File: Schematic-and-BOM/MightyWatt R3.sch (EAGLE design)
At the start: 93 parts, among them IC1 TLV271IDBVR, IC2 MAX4619EUE, IC3 OPA365AIDBVR, IC4 TS5A3166, IC5 INA225, IC6 ADS1115IDGST, IC7 TLV2372IDGK, IC8 AD5691RAD5691R, IC9 LM2766M6, T1 IXTH75N10L2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

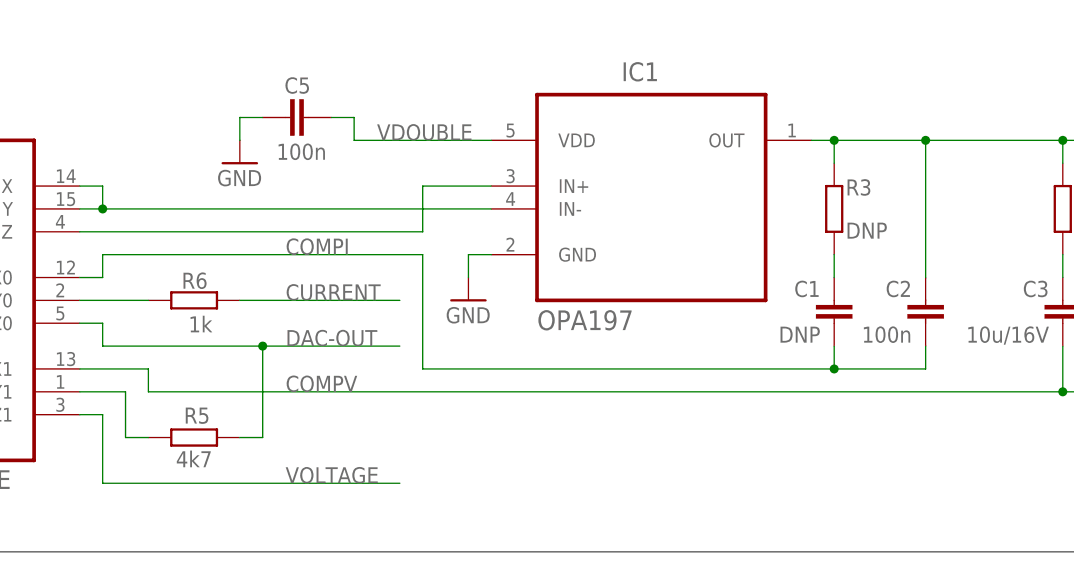
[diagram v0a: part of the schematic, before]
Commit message: Fixed schematic
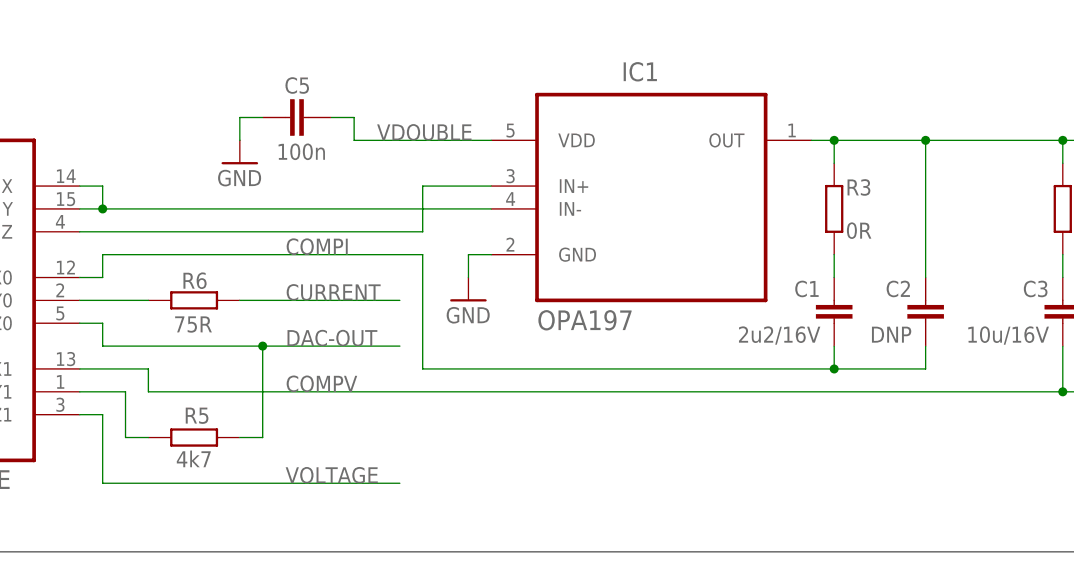
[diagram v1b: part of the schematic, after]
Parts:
- C1: value DNP -> 2u2/16V
- C2: value 100n -> DNP
- R3: value DNP -> 0R
- R6: value 1k -> 75R
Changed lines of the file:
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@@
 <part name="X1" library="con-wago-500-modified" deviceset="W237-4" device=""/>
 <part name="R5" library="rcl" deviceset="R-EU_" device="R0603" value="4k7"/>
-<part name="R6" library="rcl" deviceset="R-EU_" device="R0603" value="1k"/>
+<part name="R6" library="rcl" deviceset="R-EU_" device="R0603" value="75R"/>
 <part name="IC8" library="r2.5-3" deviceset="AD5691R" device="AD5691R"/>
 <part name="VREF1" library="supply2" deviceset="+UB" device=""/>
@@
 <part name="IC2" library="kaktus" deviceset="MAX4619EUE" device=""/>
 <part name="GND30" library="supply1" deviceset="GND" device=""/>
-<part name="C2" library="rcl" deviceset="C-EU" device="C0603" value="100n"/>
-<part name="R3" library="rcl" deviceset="R-EU_" device="R0603" value="DNP"/>
-<part name="C1" library="rcl" deviceset="C-EU" device="C1206" value="DNP"/>
+<part name="C2" library="rcl" deviceset="C-EU" device="C0603" value="DNP"/>
+<part name="R3" library="rcl" deviceset="R-EU_" device="R0603" value="0R"/>
+<part name="C1" library="rcl" deviceset="C-EU" device="C1206" value="2u2/16V"/>
 <part name="VCC1" library="supply1" deviceset="VCCIO" device=""/>
 </parts>

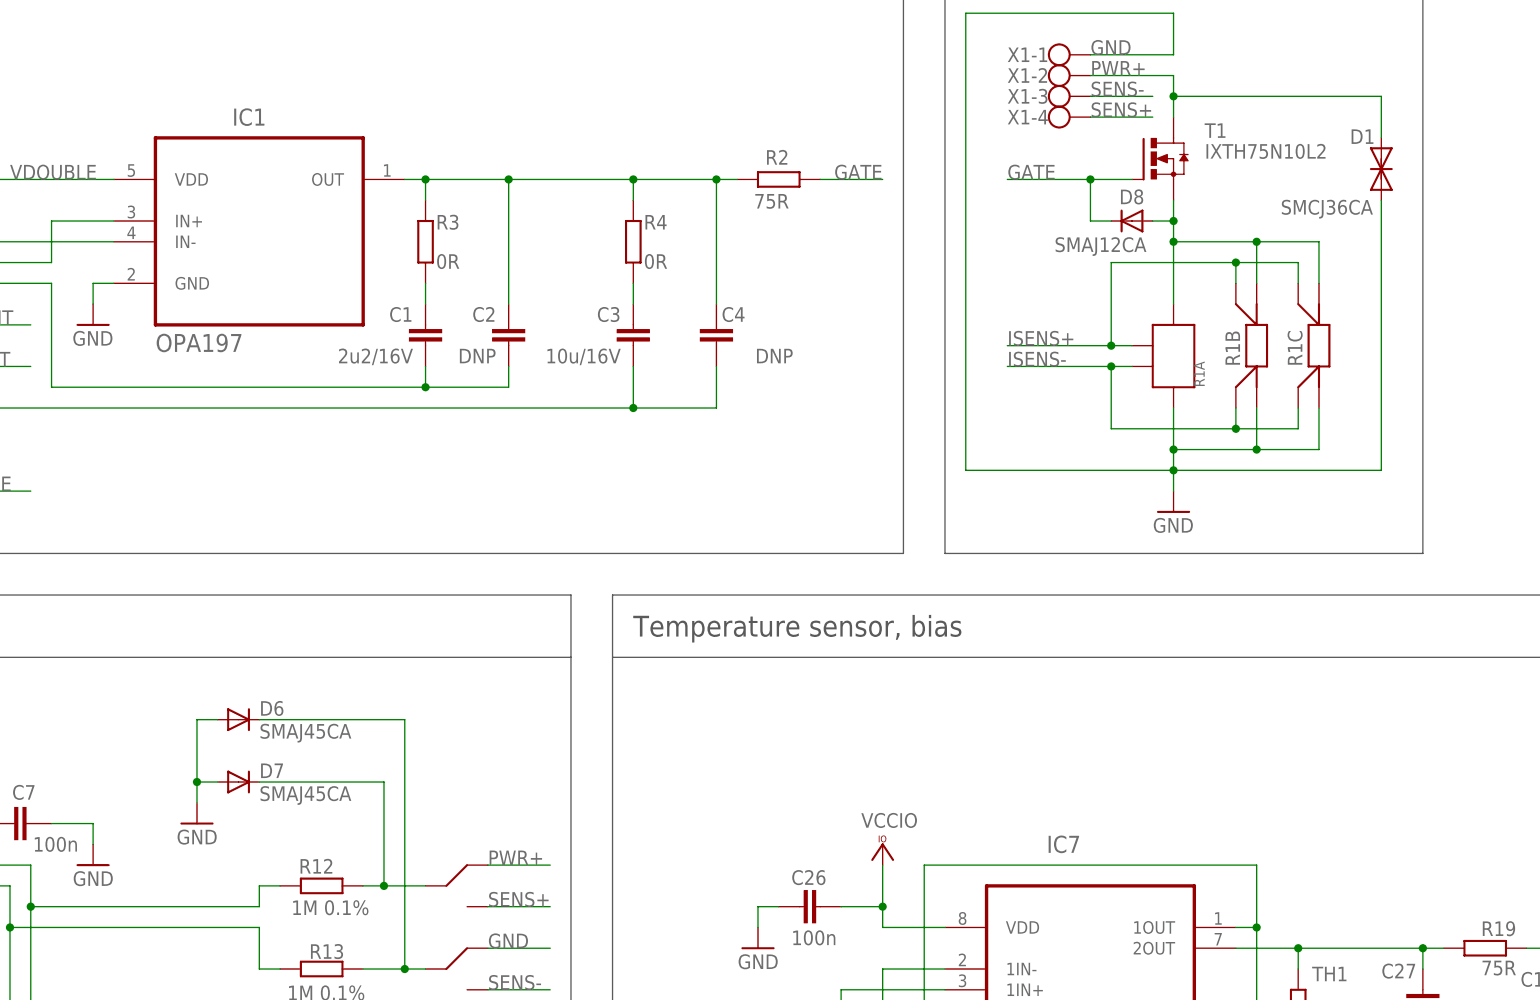
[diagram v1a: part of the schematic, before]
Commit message: Schematic fix
- Proper symbols of bi-directional TVS were added to the schematic.
- Order of switching current and voltage ranges was upgraded to decrease
spikes.
- Guide was updated.
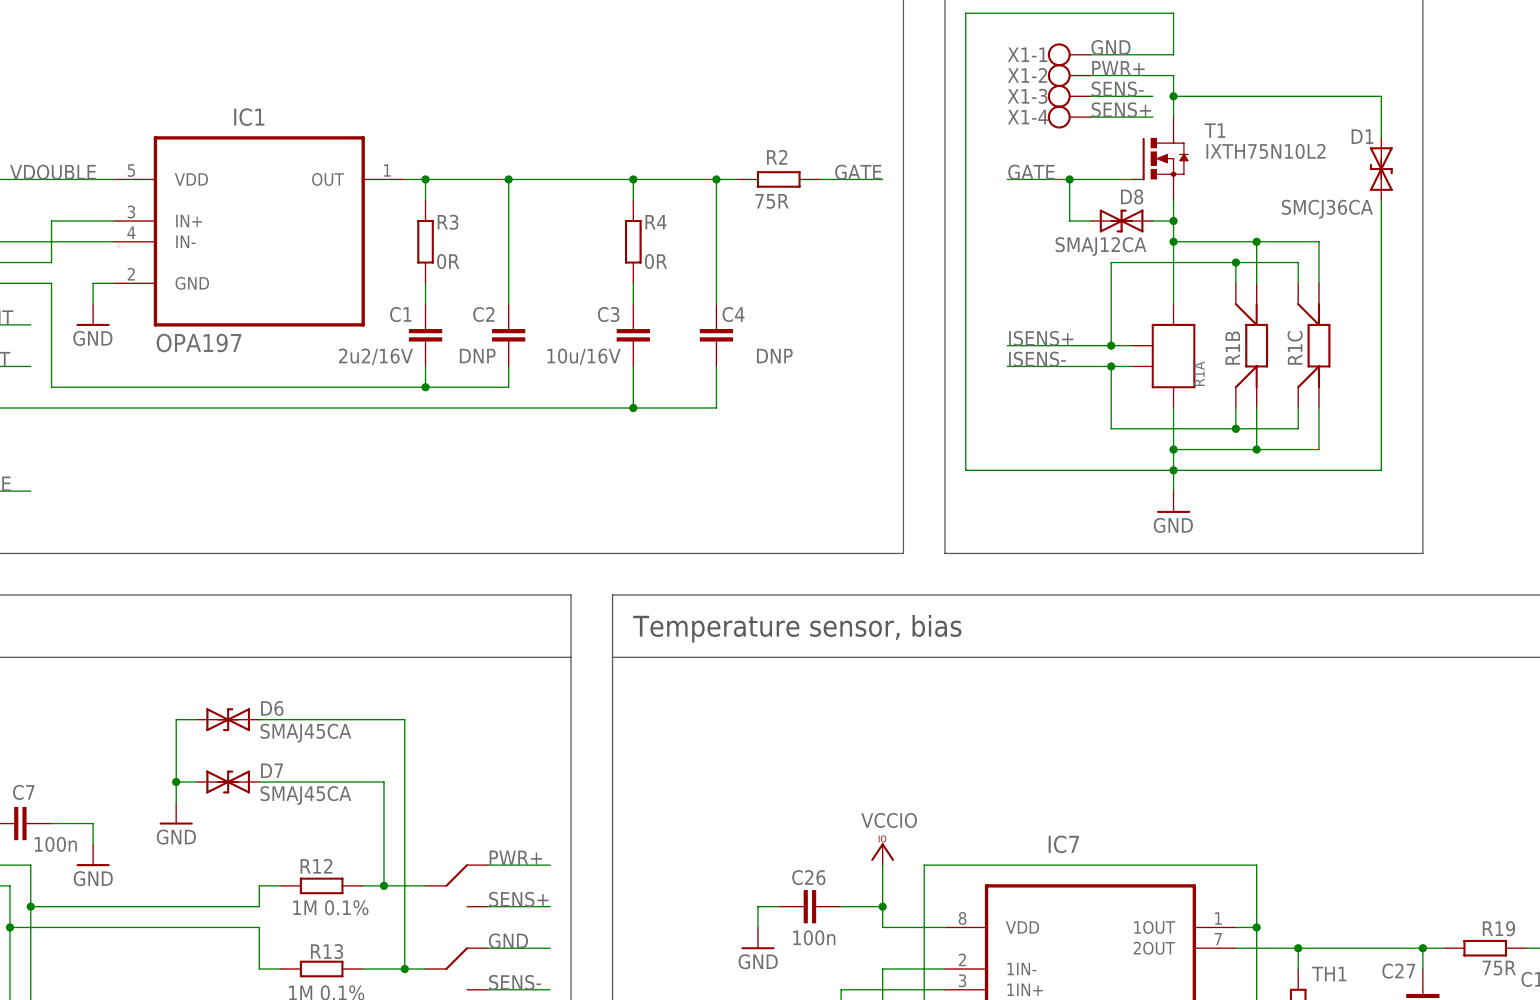
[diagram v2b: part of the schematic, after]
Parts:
- D1: device diode-tvs:DIODE-SMC -> kaktus:DIODE2SMC
- D6, D7, D8: device diode:DIODE-DO-214AC -> kaktus:DIODE2DO-214AC
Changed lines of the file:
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@@
 </classes>
 <parts>
-<part name="D1" library="diode-tvs" deviceset="DIODE-" device="SMC" value="SMCJ36CA"/>
+<part name="D1" library="kaktus" deviceset="DIODE2" device="SMC" value="SMCJ36CA"/>
 <part name="GND3" library="supply1" deviceset="GND" device=""/>
 <part name="GND4" library="supply1" deviceset="GND" device=""/>
@@
 <attribute name="MPN" value="OPA197"/>
 </part>
-<part name="D6" library="diode" deviceset="DIODE-" device="DO-214AC" value="SMAJ45CA"/>
-<part name="D7" library="diode" deviceset="DIODE-" device="DO-214AC" value="SMAJ45CA"/>
+<part name="D6" library="kaktus" deviceset="DIODE2" device="DO-214AC" value="SMAJ45CA"/>
+<part name="D7" library="kaktus" deviceset="DIODE2" device="DO-214AC" value="SMAJ45CA"/>
 <part name="GND23" library="supply1" deviceset="GND" device=""/>
 <part name="R23" library="rcl" deviceset="R-EU_" device="R0603" value="39k 0.1%"/>
@@
 <part name="GND35" library="supply1" deviceset="GND" device=""/>
 <part name="GND10" library="supply1" deviceset="GND" device=""/>
-<part name="D8" library="diode" deviceset="DIODE-" device="DO-214AC" value="SMAJ12CA"/>
+<part name="D8" library="kaktus" deviceset="DIODE2" device="DO-214AC" value="SMAJ12CA"/>
 <part name="R1B" library="kaktus" deviceset="LVK24" device=""/>
 <part name="R1C" library="kaktus" deviceset="LVK12" device=""/>
@@
 <attribute name="NAME" x="220.1926" y="235.1786" size="2.0828" layer="95" ratio="10" rot="SR0"/>
 </instance>
-<instance part="D6" gate="G$1" x="220.98" y="162.56"/>
-<instance part="D7" gate="G$1" x="220.98" y="154.94"/>
-<instance part="GND23" gate="1" x="215.9" y="149.86" rot="MR0"/>
+<instance part="D6" gate="G$1" x="218.44" y="162.56"/>
+<instance part="D7" gate="G$1" x="218.44" y="154.94"/>
+<instance part="GND23" gate="1" x="213.36" y="149.86" rot="MR0"/>
 <instance part="R23" gate="G$1" x="279.4" y="111.76" smashed="yes" rot="MR90">
 <attribute name="NAME" x="278.13" y="115.7986" size="1.778" layer="95" rot="MR0"/>
@@
 <segment>
 <pinref part="GND23" gate="1" pin="GND"/>
-<wire x1="215.9" y1="162.56" x2="215.9" y2="154.94" width="0.1524" layer="91"/>
+<wire x1="213.36" y1="162.56" x2="213.36" y2="154.94" width="0.1524" layer="91"/>
 <pinref part="D6" gate="G$1" pin="A"/>
-<wire x1="215.9" y1="154.94" x2="215.9" y2="152.4" width="0.1524" layer="91"/>
-<wire x1="218.44" y1="162.56" x2="215.9" y2="162.56" width="0.1524" layer="91"/>
+<wire x1="213.36" y1="154.94" x2="213.36" y2="152.4" width="0.1524" layer="91"/>
+<wire x1="215.9" y1="162.56" x2="213.36" y2="162.56" width="0.1524" layer="91"/>
 <pinref part="D7" gate="G$1" pin="A"/>
-<wire x1="218.44" y1="154.94" x2="215.9" y2="154.94" width="0.1524" layer="91"/>
-<junction x="215.9" y="154.94"/>
+<wire x1="215.9" y1="154.94" x2="213.36" y2="154.94" width="0.1524" layer="91"/>
+<junction x="213.36" y="154.94"/>
 </segment>
 <segment>
@@
 </segment>
 <segment>
-<wire x1="330.2" y1="228.6" x2="325.12" y2="228.6" width="0.1524" layer="91"/>
+<wire x1="330.2" y1="228.6" x2="322.58" y2="228.6" width="0.1524" layer="91"/>
 <label x="314.96" y="228.6" size="1.778" layer="95"/>
 <pinref part="T1" gate="G$1" pin="G"/>
-<wire x1="325.12" y1="228.6" x2="314.96" y2="228.6" width="0.1524" layer="91"/>
-<wire x1="327.66" y1="223.52" x2="325.12" y2="223.52" width="0.1524" layer="91"/>
-<wire x1="325.12" y1="223.52" x2="325.12" y2="228.6" width="0.1524" layer="91"/>
-<junction x="325.12" y="228.6"/>
+<wire x1="322.58" y1="228.6" x2="314.96" y2="228.6" width="0.1524" layer="91"/>
+<wire x1="325.12" y1="223.52" x2="322.58" y2="223.52" width="0.1524" layer="91"/>
+<wire x1="322.58" y1="223.52" x2="322.58" y2="228.6" width="0.1524" layer="91"/>
+<junction x="322.58" y="228.6"/>
 <pinref part="D8" gate="G$1" pin="C"/>
 </segment>
